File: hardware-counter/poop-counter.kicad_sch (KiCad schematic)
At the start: 29 parts, among them J1 USB_C_Receptacle_USB2.0, J2 RJ45_LED, U0 ESP8266EX, U1 AMS1117-3.3, U2 CP2102N-A01-GQFN24, U3 MAX485E, U4 W25Q32JVSS, Y1 24Mhz±10ppm

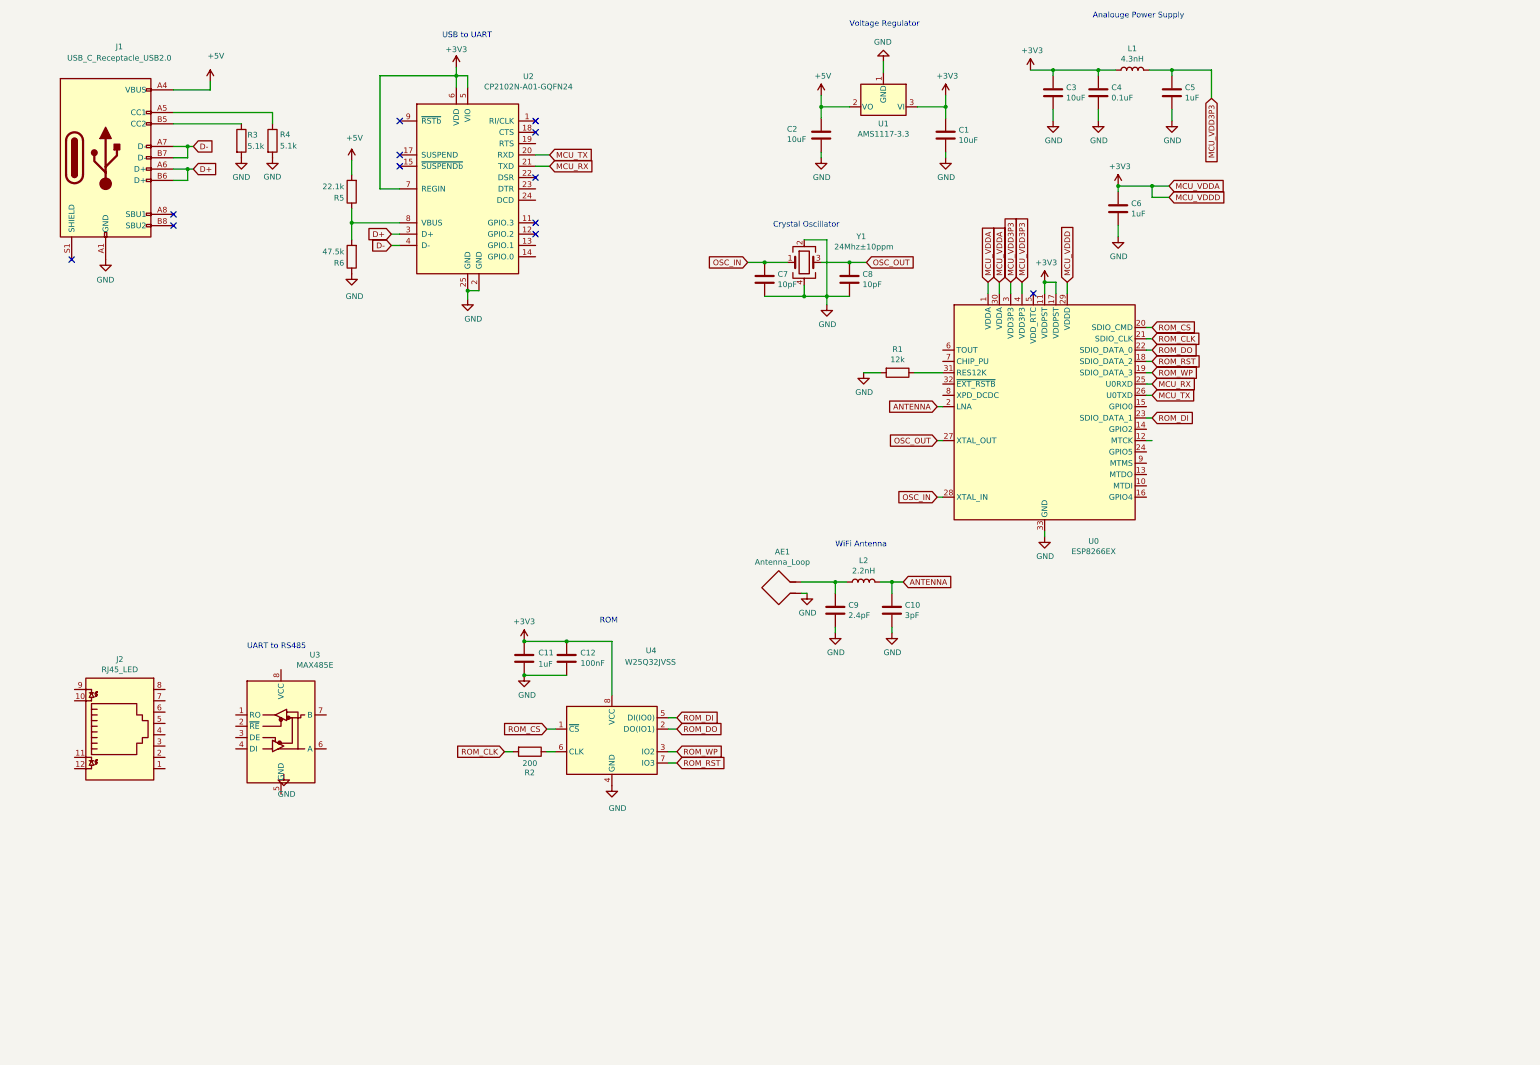
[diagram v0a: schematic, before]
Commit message: finish PCB schem
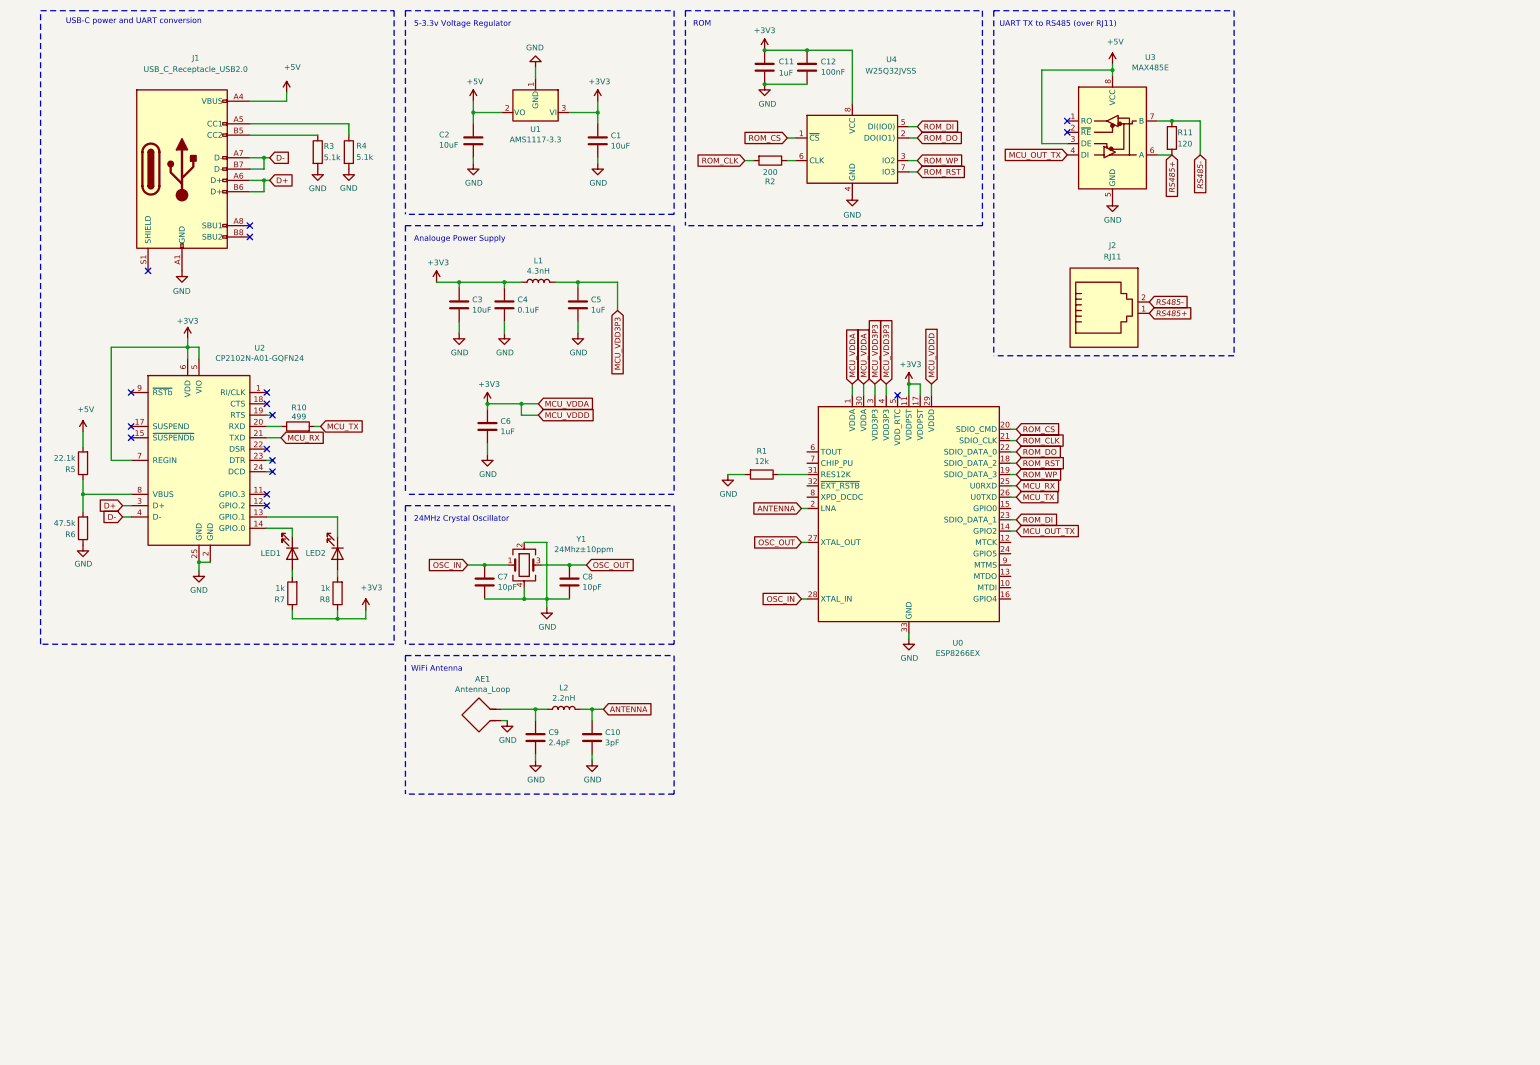
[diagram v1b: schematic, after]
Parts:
- removed J2: RJ45_LED, symbol Connector:RJ45_LED
- added D?: LED2, symbol Device:LED
- added D?: LED1, symbol Device:LED
- added J2: RJ11, symbol Connector:RJ11
- added R10: 499, symbol Device:R
- added R11: 120, symbol Device:R
- added R7, R8: 1k, symbol Device:R
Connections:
- net +3V3: now also R7.1, R8.1
- net +5V: now also U3.3 (DE), U3.8 (VCC)
- net GND: now also U3.5 (GND)
- net MCU_TX: now also R10.2; no longer U2.20 (RXD)
- net MCU_OUT_TX: now reaches U0.14 (GPIO2)
- net MCU_OUT_TX: now also U3.4 (DI)
- net at U2.13 (GPIO.1): now also D?.1 (K)
- net at U2.14 (GPIO.0): now also D?.1 (K)
- net RS485+: now reaches U3.6 (A)
- net RS485+: now also J2.1, R11.2
- net RS485-: now reaches U3.7 (B)
- net RS485-: now also J2.2, R11.1
- new net: R10.1, U2.20 (RXD)
- new net: D?.2 (A), R7.2
- new net: D?.2 (A), R8.2
- no-connect marks 12 -> 17
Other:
- note added: "24MHz Crystal Oscillator"
- note added: "5-3.3v Voltage Regulator"
- note added: "UART TX to RS485 (over RJ11)"
- note added: "USB-C power and UART conversion"
- note removed: "Crystal Oscillator"
- note removed: "UART to RS485"
- note removed: "USB to UART"
- note removed: "Voltage Regulator"
- moved on the sheet: AE1, C1, C10, C11, C12, C2, C3, C4, C5, C6, C7, C8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

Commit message: footprint moment
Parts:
- removed J2: RJ11, symbol Connector:RJ11
- added J2: RJ12, Connector_RJ:RJ12_Amphenol_54601, symbol Connector:RJ12
- AE1: footprint (none) -> RF_Antenna:Texas_SWRA117D_2.4GHz_Right
- C1, C10, C11, C12, C2, C3, C4, C5, C6, C7, C8, C9: footprint (none) -> Capacitor_SMD:C_0805_2012Metric_Pad1.18x1.45mm_HandSolder
- D1, D2: renamed from D?; footprint (none) -> LED_SMD:LED_0805_2012Metric_Pad1.15x1.40mm_HandSolder
- J1: footprint (none) -> Connector_USB:USB_C_Receptacle_Palconn_UTC16-G
- L1, L2: footprint (none) -> Inductor_SMD:L_0805_2012Metric_Pad1.05x1.20mm_HandSolder
- R1, R10, R11, R2, R3, R4, R5, R6, R7, R8: footprint (none) -> Resistor_SMD:R_0805_2012Metric_Pad1.20x1.40mm_HandSolder
- U3: footprint (none) -> lib_kicad:SOIC127P600X175-8N
- Y1: footprint (none) -> Crystal:Crystal_SMD_3225-4Pin_3.2x2.5mm_HandSoldering
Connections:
- net RS485+: now also J2.2, J2.3
- net RS485-: now also J2.4, J2.5
- no-connect marks 17 -> 19
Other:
- note added: "RTS/DTR/DCD Can be used for a auto-reset feature"
- note added: "USB-C Power and UART Conversion"
- note removed: "USB-C power and UART conversion"
- moved on the sheet: AE1, C10, C9, L2

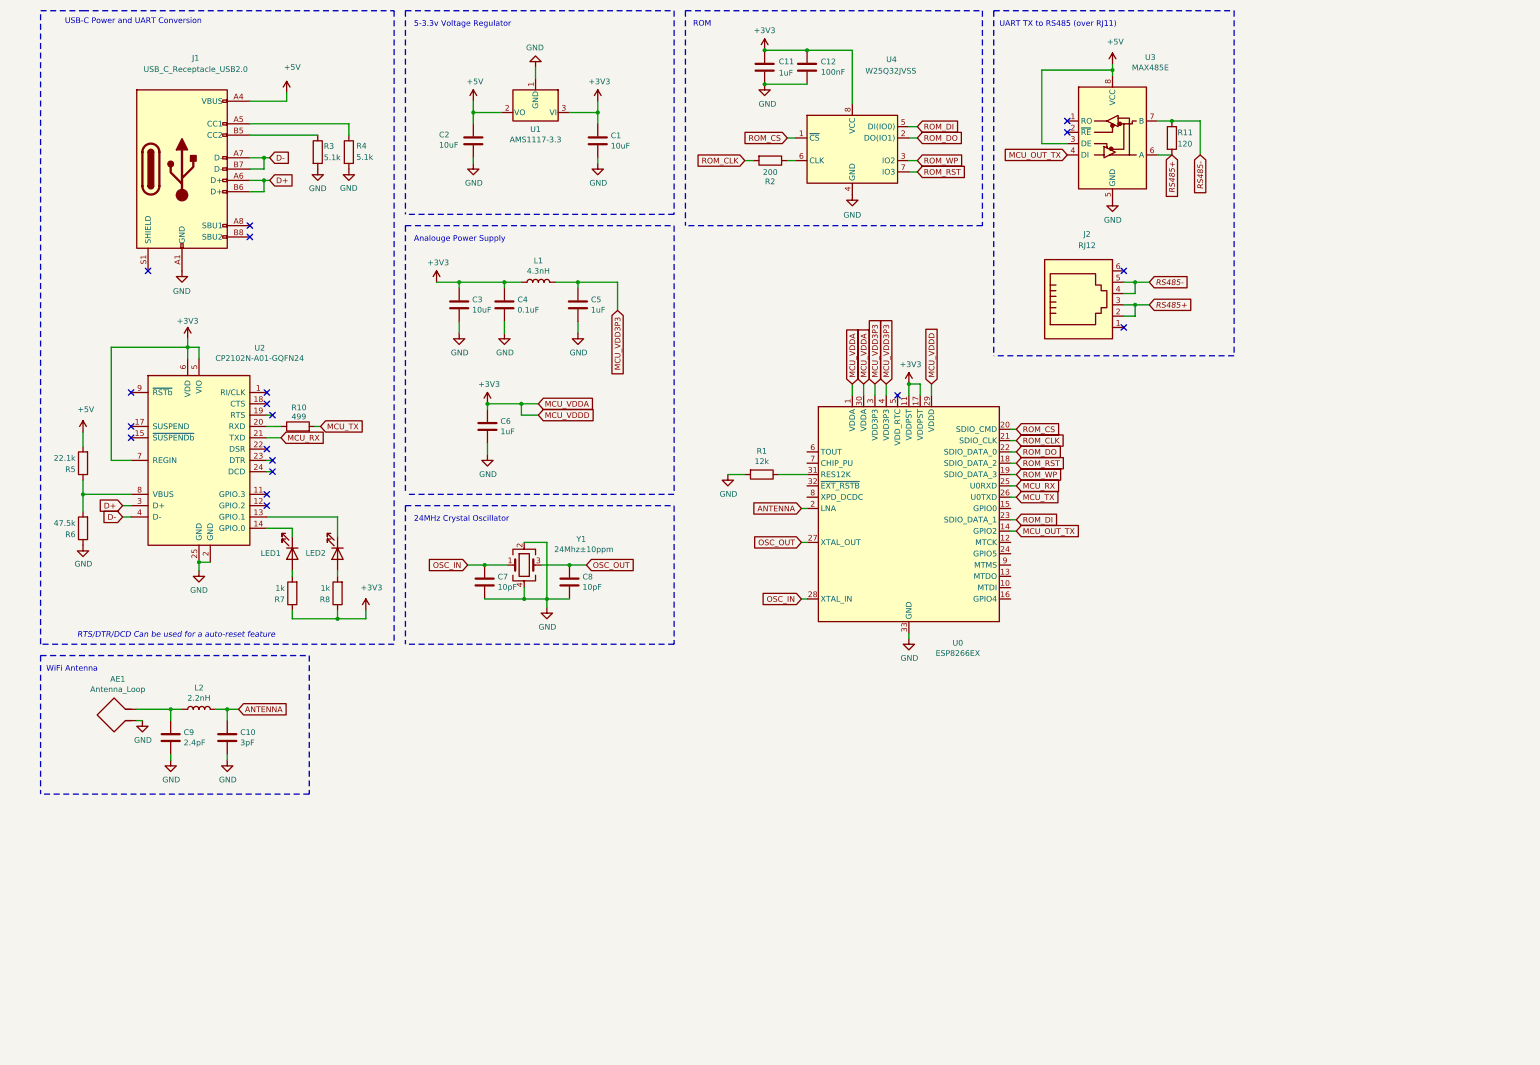
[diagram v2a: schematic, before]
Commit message: bout to remove USB
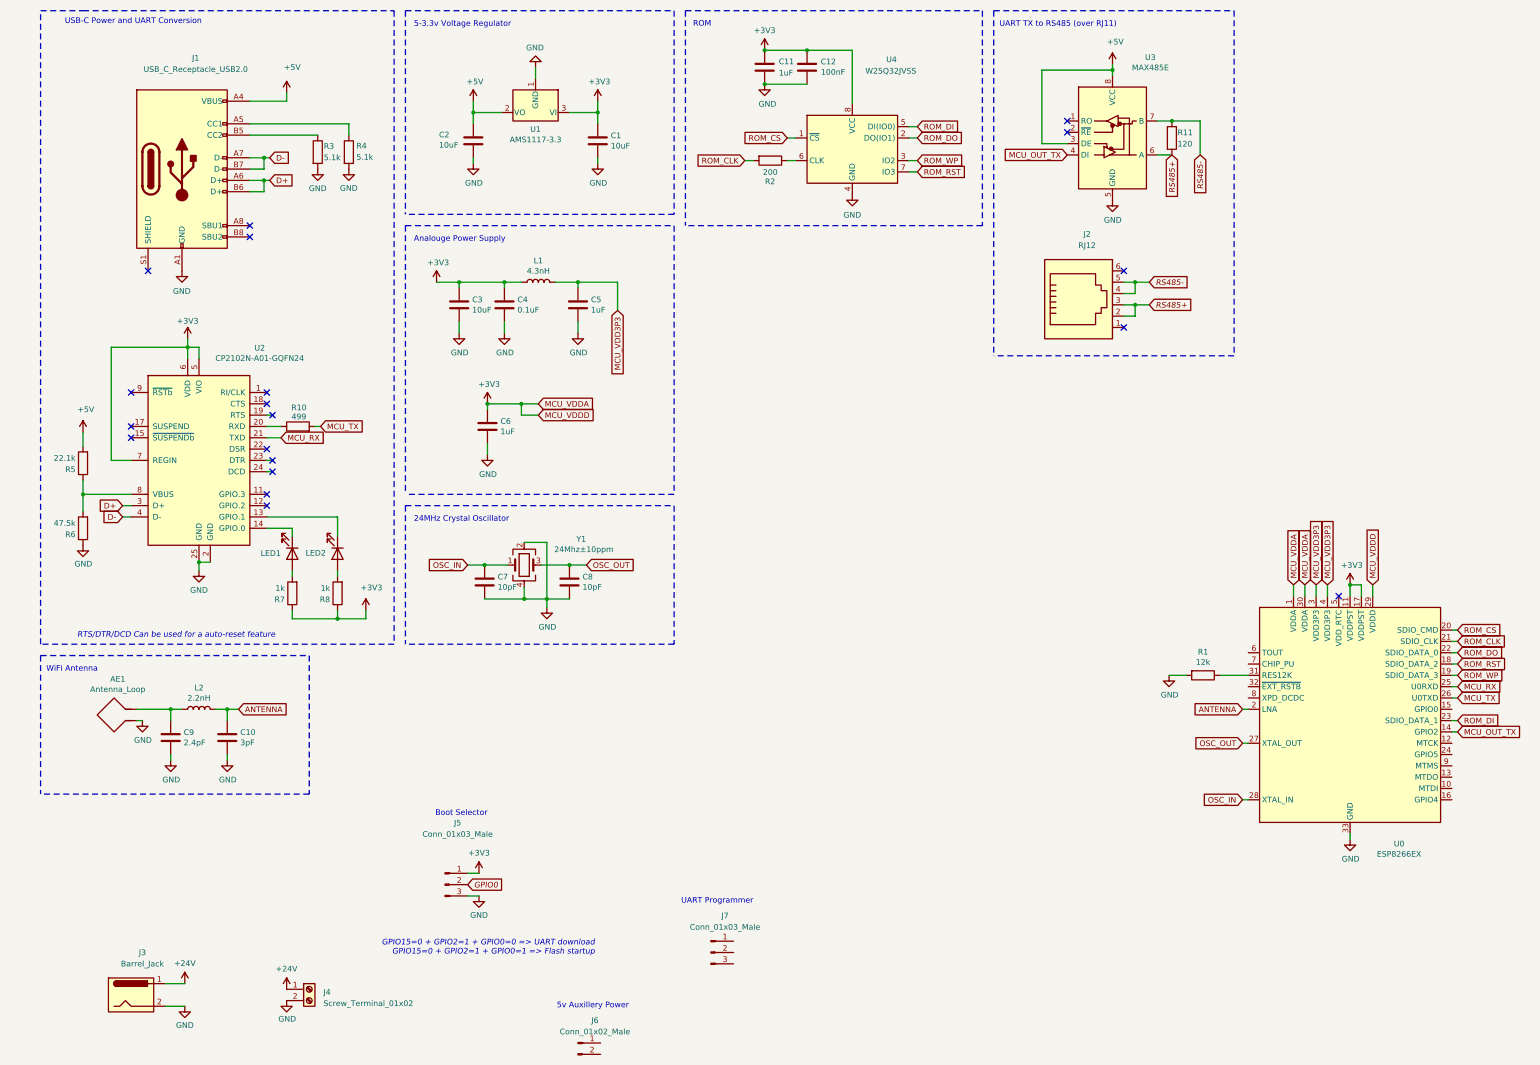
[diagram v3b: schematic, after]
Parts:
- added J3: Barrel_Jack, Connector_BarrelJack:BarrelJack_CLIFF_FC681465S_SMT_Horizontal, symbol Connector:Barrel_Jack
- added J4: Screw_Terminal_01x02, TerminalBlock:TerminalBlock_bornier-2_P5.08mm, symbol Connector:Screw_Terminal_01x02
- added J5, J7: Conn_01x03_Male, Connector_PinHeader_2.54mm:PinHeader_1x03_P2.54mm_Vertical, symbol Connector:Conn_01x03_Male
- added J6: Conn_01x02_Male, Connector_PinHeader_2.54mm:PinHeader_1x02_P2.54mm_Vertical, symbol Connector:Conn_01x02_Male
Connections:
- net +3V3: now also J5.1 (Pin_1)
- net GND: now also J3.2, J4.2 (Pin_2), J5.3 (Pin_3)
- new net +24V: J3.1, J4.1 (Pin_1)
- new net GPIO0: J5.2 (Pin_2)
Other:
- note added: "5v Auxillery Power"
- note added: "Boot Selector"
- note added: "GPIO15=0 + GPIO2=1 + GPIO0=0 => UART download GPIO15=0 + GPIO2=1 + GPIO0=1 => Flash startup"
- note added: "UART Programmer"
- moved on the sheet: R1, U0

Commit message: done v1, need to redo routing entirely lol
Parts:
- removed D1: LED1, LED_SMD:LED_0805_2012Metric_Pad1.15x1.40mm_HandSolder, symbol Device:LED
- removed D2: LED2, LED_SMD:LED_0805_2012Metric_Pad1.15x1.40mm_HandSolder, symbol Device:LED
- removed J1: USB_C_Receptacle_USB2.0, Connector_USB:USB_C_Receptacle_Palconn_UTC16-G, symbol Connector:USB_C_Receptacle_USB2.0
- removed R10: 499, Resistor_SMD:R_0805_2012Metric_Pad1.20x1.40mm_HandSolder, symbol Device:R
- removed R4: 5.1k, Resistor_SMD:R_0805_2012Metric_Pad1.20x1.40mm_HandSolder, symbol Device:R
- removed R5: 22.1k, Resistor_SMD:R_0805_2012Metric_Pad1.20x1.40mm_HandSolder, symbol Device:R
- removed R6: 47.5k, Resistor_SMD:R_0805_2012Metric_Pad1.20x1.40mm_HandSolder, symbol Device:R
- removed R7, R8: 1k, Resistor_SMD:R_0805_2012Metric_Pad1.20x1.40mm_HandSolder, symbol Device:R
- removed U2: CP2102N-A01-GQFN24, Package_DFN_QFN:QFN-24-1EP_4x4mm_P0.5mm_EP2.6x2.6mm, symbol poop-counter-rescue:CP2102N-A01-GQFN24-Interface_USB
- added C13: 0.33uF, Capacitor_SMD:C_0805_2012Metric_Pad1.18x1.45mm_HandSolder, symbol Device:C
- added C14: 0.1uF, Capacitor_SMD:C_0805_2012Metric_Pad1.18x1.45mm_HandSolder, symbol Device:C
- added U5: LM7805_TO220, Package_TO_SOT_THT:TO-220-3_Vertical, symbol Regulator_Linear:LM7805_TO220
- R3: value 5.1k -> 1k
- Y1: footprint Crystal:Crystal_SMD_3225-4Pin_3.2x2.5mm_HandSoldering -> Crystal:Crystal_SMD_EuroQuartz_X22-4Pin_2.5x2.0mm
- renumbered C2 to C1, C1 to C2, J2 to J1, J5 to J2, J7 to J3, J6 to J4, J4 to J5, J3 to J6, R11 to R1, R1 to R2, R2 to R4, U3 to U2
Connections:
- net +24V: now also C13.2, U5.1 (VI)
- net +3V3: now also R3.2, U0.14 (GPIO2)
- net +5V: now also J4.1 (Pin_1), C14.1, U5.3 (VO)
- net GND: now also J3.3 (Pin_3), J4.2 (Pin_2), U0.13 (MTDO), C13.1, C14.2, U5.2 (GND); no longer R3.2
- net GPIO0: now also R3.1, U0.15 (GPIO0)
- net MCU_RX: now also J3.1 (Pin_1)
- net MCU_TX: now also J3.2 (Pin_2), U2.4 (DI)
- removed net MCU_OUT_TX: U0.14 (GPIO2), U2.4 (DI)
- no-connect marks 19 -> 14
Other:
- note added: "GPIO15(MTDO)=0 + GPIO2=1 + GPIO0=0 => UART download GPIO15(MTDO)=0 + GPIO2=1 + GPIO0=1 => Flash startup Requires jumper, can be bridged in production"
- note removed: "GPIO15=0 + GPIO2=1 + GPIO0=0 => UART download GPIO15=0 + GPIO2=1 + GPIO0=1 => Flash startup"
- note removed: "RTS/DTR/DCD Can be used for a auto-reset feature"
- note removed: "USB-C Power and UART Conversion"
- moved on the sheet: C1, C11, C12, C2, C3, C4, C5, C6, C7, C8, J1, J2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
